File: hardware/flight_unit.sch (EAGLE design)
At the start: 26 parts, among them IC2 7805T, J2 CONN_20X2SHROUDED, T1 THERMISTOR-2,5, U1 4MB Flash, U2 4MB Flash, U3 4MB Flash

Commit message: Add files via upload
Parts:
- added X1, X2: S4B-ZR, con-jst:S4B-ZR
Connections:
- net GND: now also X1-2.1, X2-2.1
- net N$1: now also X1-1.1
- net N$4: now also X2-1.1
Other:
- moved on the sheet: D1
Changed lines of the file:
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@@
 <part name="C2" library="capacitor-wima" library_urn="urn:adsk.eagle:library:116" deviceset="C" device="2,5-3" package3d_urn="urn:adsk.eagle:package:5436/1" value="0.1uf"/>
 <part name="GND2" library="SparkFun-PowerSymbols" library_urn="urn:adsk.eagle:library:530" deviceset="GND" device=""/>
+<part name="X1" library="con-jst" library_urn="urn:adsk.eagle:library:156" deviceset="?4B-ZR" device="S" package3d_urn="urn:adsk.eagle:package:7641/1"/>
+<part name="X2" library="con-jst" library_urn="urn:adsk.eagle:library:156" deviceset="?4B-ZR" device="S" package3d_urn="urn:adsk.eagle:package:7641/1"/>
+<part name="GND9" library="SparkFun-PowerSymbols" library_urn="urn:adsk.eagle:library:530" deviceset="GND" device=""/>
+<part name="GND10" library="SparkFun-PowerSymbols" library_urn="urn:adsk.eagle:library:530" deviceset="GND" device=""/>
 </parts>
 <sheets>
@@
 </text>
 <text x="82.55" y="161.29" size="5.08" layer="97">Power Regulation and Supply</text>
-<text x="68.58" y="109.22" size="1.778" layer="91">ISS Power Source</text>
-<text x="114.3" y="81.28" size="1.778" layer="91">Backup Battery Input </text>
+<text x="78.74" y="116.84" size="1.778" layer="91">ISS Power Source</text>
+<text x="106.68" y="76.2" size="1.778" layer="91">Backup Battery Input </text>
 </plain>
 <instances>
@@
 <attribute name="SHEET" x="230.505" y="5.08" size="2.54" layer="94"/>
 </instance>
-<instance part="D1" gate="1" x="105.41" y="110.49" smashed="yes">
-<attribute name="NAME" x="107.95" y="110.9726" size="1.778" layer="95"/>
-<attribute name="VALUE" x="107.95" y="108.1786" size="1.778" layer="96"/>
+<instance part="D1" gate="1" x="110.49" y="110.49" smashed="yes">
+<attribute name="NAME" x="113.03" y="110.9726" size="1.778" layer="95"/>
+<attribute name="VALUE" x="113.03" y="108.1786" size="1.778" layer="96"/>
 </instance>
 <instance part="D2" gate="1" x="129.54" y="100.33" smashed="yes" rot="R90">
@@
 <instance part="GND2" gate="1" x="134.62" y="93.98" smashed="yes">
 <attribute name="VALUE" x="134.62" y="93.726" size="1.778" layer="96" align="top-center"/>
+</instance>
+<instance part="X1" gate="-1" x="116.84" y="86.36" smashed="yes" rot="MR0">
+<attribute name="NAME" x="115.824" y="85.598" size="1.524" layer="95" rot="MR0"/>
+<attribute name="VALUE" x="120.904" y="87.884" size="1.778" layer="96" rot="MR0"/>
+</instance>
+<instance part="X1" gate="-2" x="116.84" y="83.82" smashed="yes" rot="MR0">
+<attribute name="NAME" x="115.824" y="83.058" size="1.524" layer="95" rot="MR0"/>
+</instance>
+<instance part="X2" gate="-1" x="88.9" y="111.76" smashed="yes" rot="MR0">
+<attribute name="NAME" x="87.884" y="110.998" size="1.524" layer="95" rot="MR0"/>
+<attribute name="VALUE" x="92.964" y="113.284" size="1.778" layer="96" rot="MR0"/>
+</instance>
+<instance part="X2" gate="-2" x="88.9" y="109.22" smashed="yes" rot="MR0">
+<attribute name="NAME" x="87.884" y="108.458" size="1.524" layer="95" rot="MR0"/>
+</instance>
+<instance part="GND9" gate="1" x="96.52" y="106.68" smashed="yes">
+<attribute name="VALUE" x="96.52" y="106.426" size="1.778" layer="96" align="top-center"/>
+</instance>
+<instance part="GND10" gate="1" x="121.92" y="81.28" smashed="yes">
+<attribute name="VALUE" x="121.92" y="81.026" size="1.778" layer="96" align="top-center"/>
 </instance>
 </instances>
@@
 <wire x1="121.92" y1="95.25" x2="129.54" y2="95.25" width="0.1524" layer="91"/>
 <wire x1="129.54" y1="95.25" x2="129.54" y2="97.79" width="0.1524" layer="91"/>
-<wire x1="121.92" y1="95.25" x2="121.92" y2="83.82" width="0.1524" layer="91"/>
+<pinref part="X1" gate="-1" pin="1"/>
+<wire x1="121.92" y1="86.36" x2="121.92" y2="95.25" width="0.1524" layer="91"/>
 <junction x="121.92" y="95.25"/>
 </segment>
@@
 <pinref part="D1" gate="1" pin="C"/>
 <pinref part="R1" gate="G$1" pin="2"/>
-<wire x1="107.95" y1="110.49" x2="121.92" y2="110.49" width="0.1524" layer="91"/>
+<wire x1="113.03" y1="110.49" x2="121.92" y2="110.49" width="0.1524" layer="91"/>
 <wire x1="121.92" y1="110.49" x2="121.92" y2="105.41" width="0.1524" layer="91"/>
 <junction x="121.92" y="110.49"/>
@@
 </segment>
 </net>
-<net name="N$4" class="0">
-<segment>
-<pinref part="D1" gate="1" pin="A"/>
-<wire x1="91.44" y1="110.49" x2="102.87" y2="110.49" width="0.1524" layer="91"/>
-</segment>
-</net>
 <net name="+3V3" class="0">
 <segment>
@@
 <wire x1="134.62" y1="99.06" x2="134.62" y2="96.52" width="0.1524" layer="91"/>
 </segment>
+<segment>
+<pinref part="X2" gate="-2" pin="1"/>
+<pinref part="GND9" gate="1" pin="GND"/>
+<wire x1="93.98" y1="109.22" x2="96.52" y2="109.22" width="0.1524" layer="91"/>
+</segment>
+<segment>
+<pinref part="GND10" gate="1" pin="GND"/>
+<pinref part="X1" gate="-2" pin="1"/>
+</segment>
 </net>
 <net name="N$9" class="0">
@@
 </segment>
 </net>
+<net name="N$4" class="0">
+<segment>
+<pinref part="X2" gate="-1" pin="1"/>
+<pinref part="D1" gate="1" pin="A"/>
+<wire x1="93.98" y1="111.76" x2="107.95" y2="111.76" width="0.1524" layer="91"/>
+<wire x1="107.95" y1="111.76" x2="107.95" y2="110.49" width="0.1524" layer="91"/>
+</segment>
+</net>

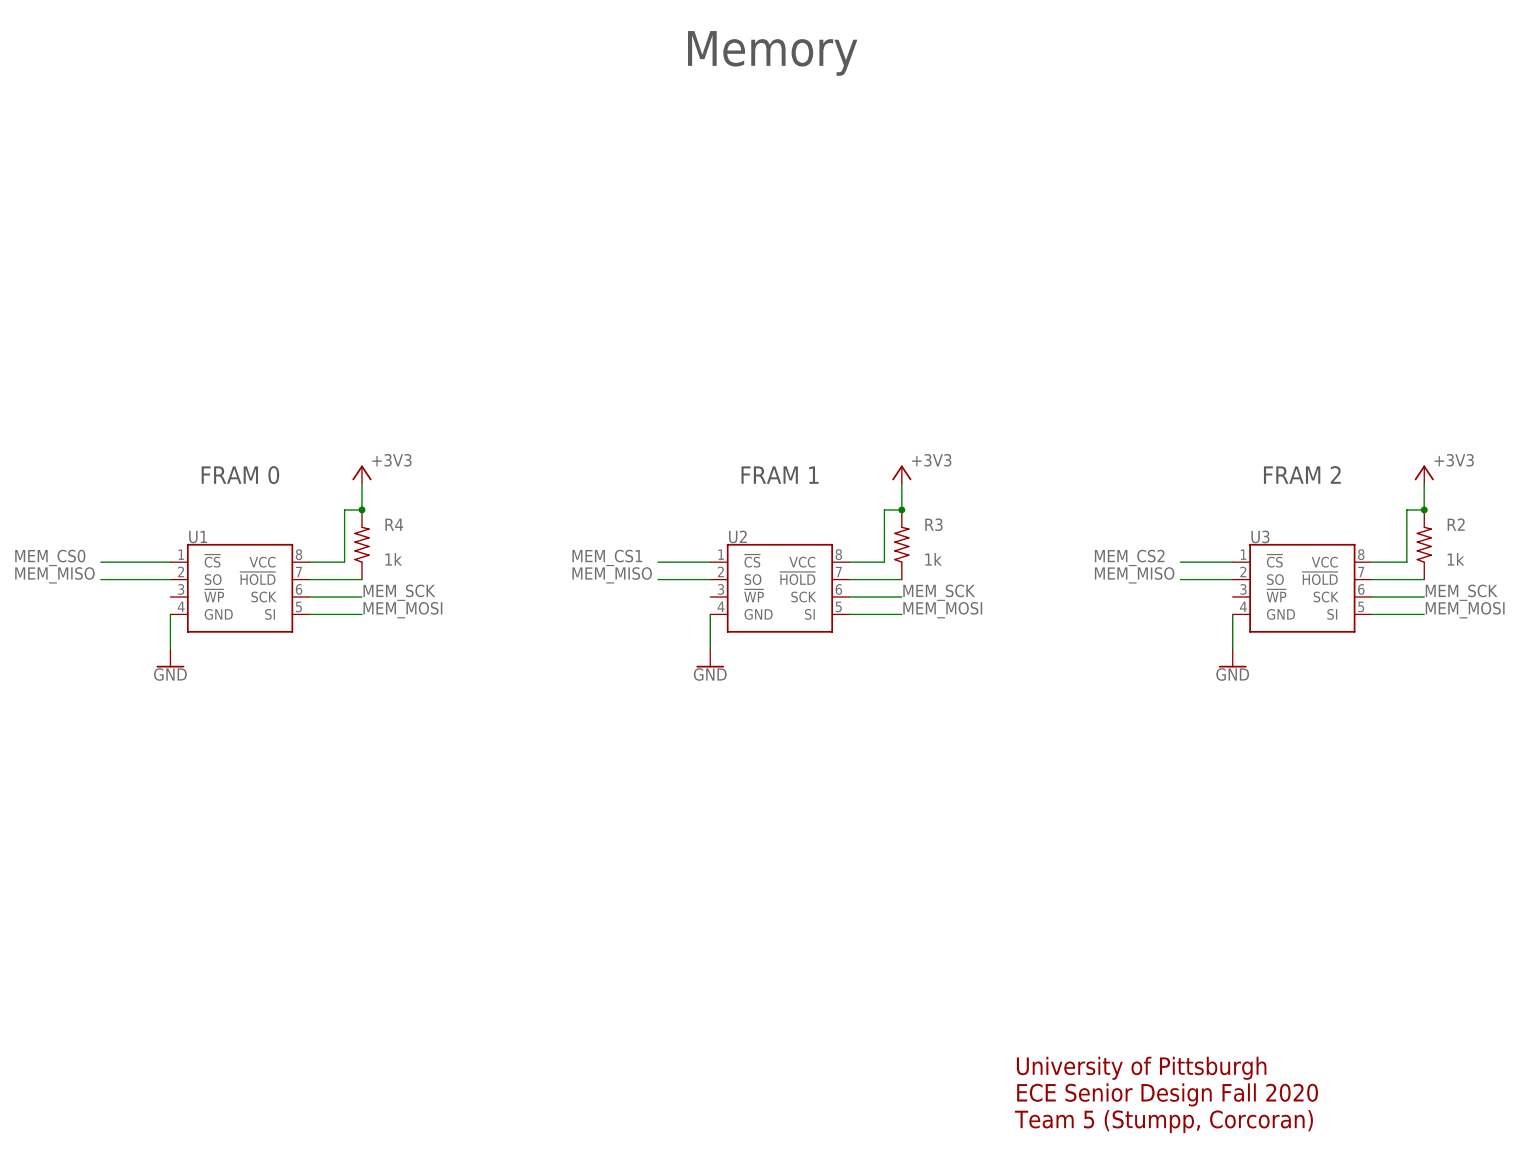
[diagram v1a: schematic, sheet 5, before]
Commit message: Added decoupling caps to memory schematic
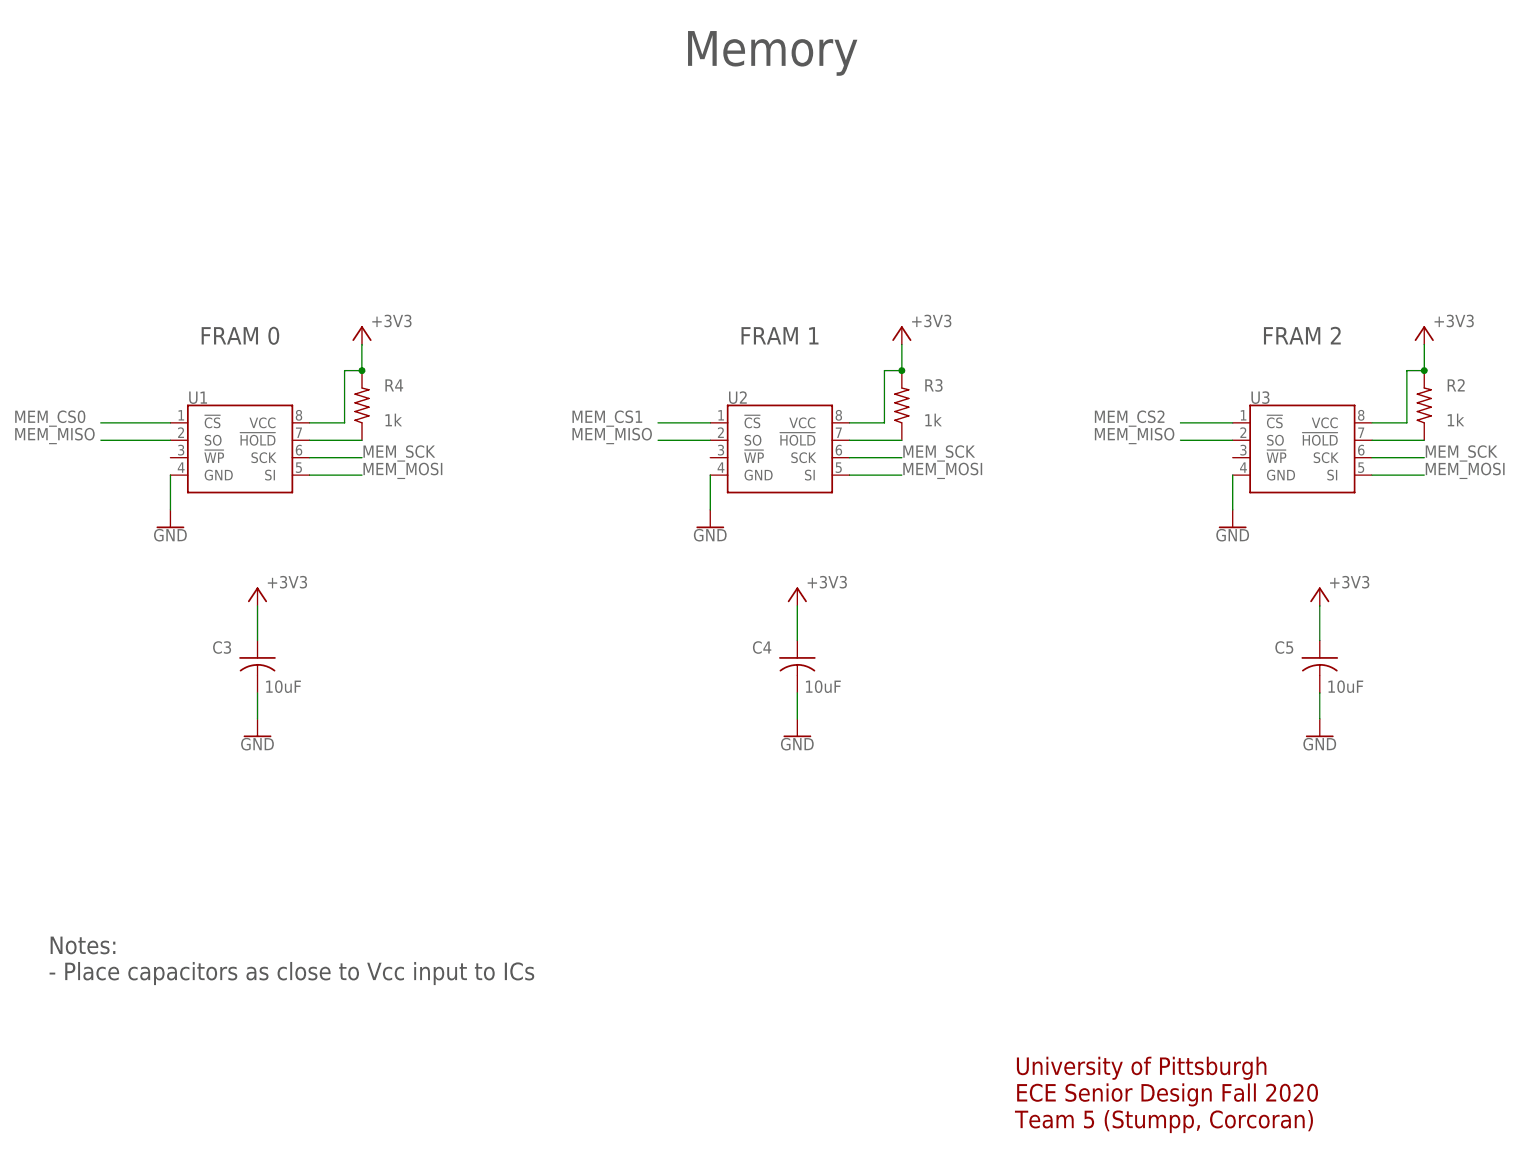
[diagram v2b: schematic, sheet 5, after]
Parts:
- added C3, C4, C5: 10uF, adafruit:C-US025-040X050
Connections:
- net +3V3: now also C3.1, C4.1, C5.1
- net GND: now also C3.2, C4.2, C5.2
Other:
- note added: "Notes: - Place capacitors as close to Vcc input to ICs"
- moved on the sheet: R2, R3, R4, U1, U2, U3

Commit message: updates to schematic and preliminary board work
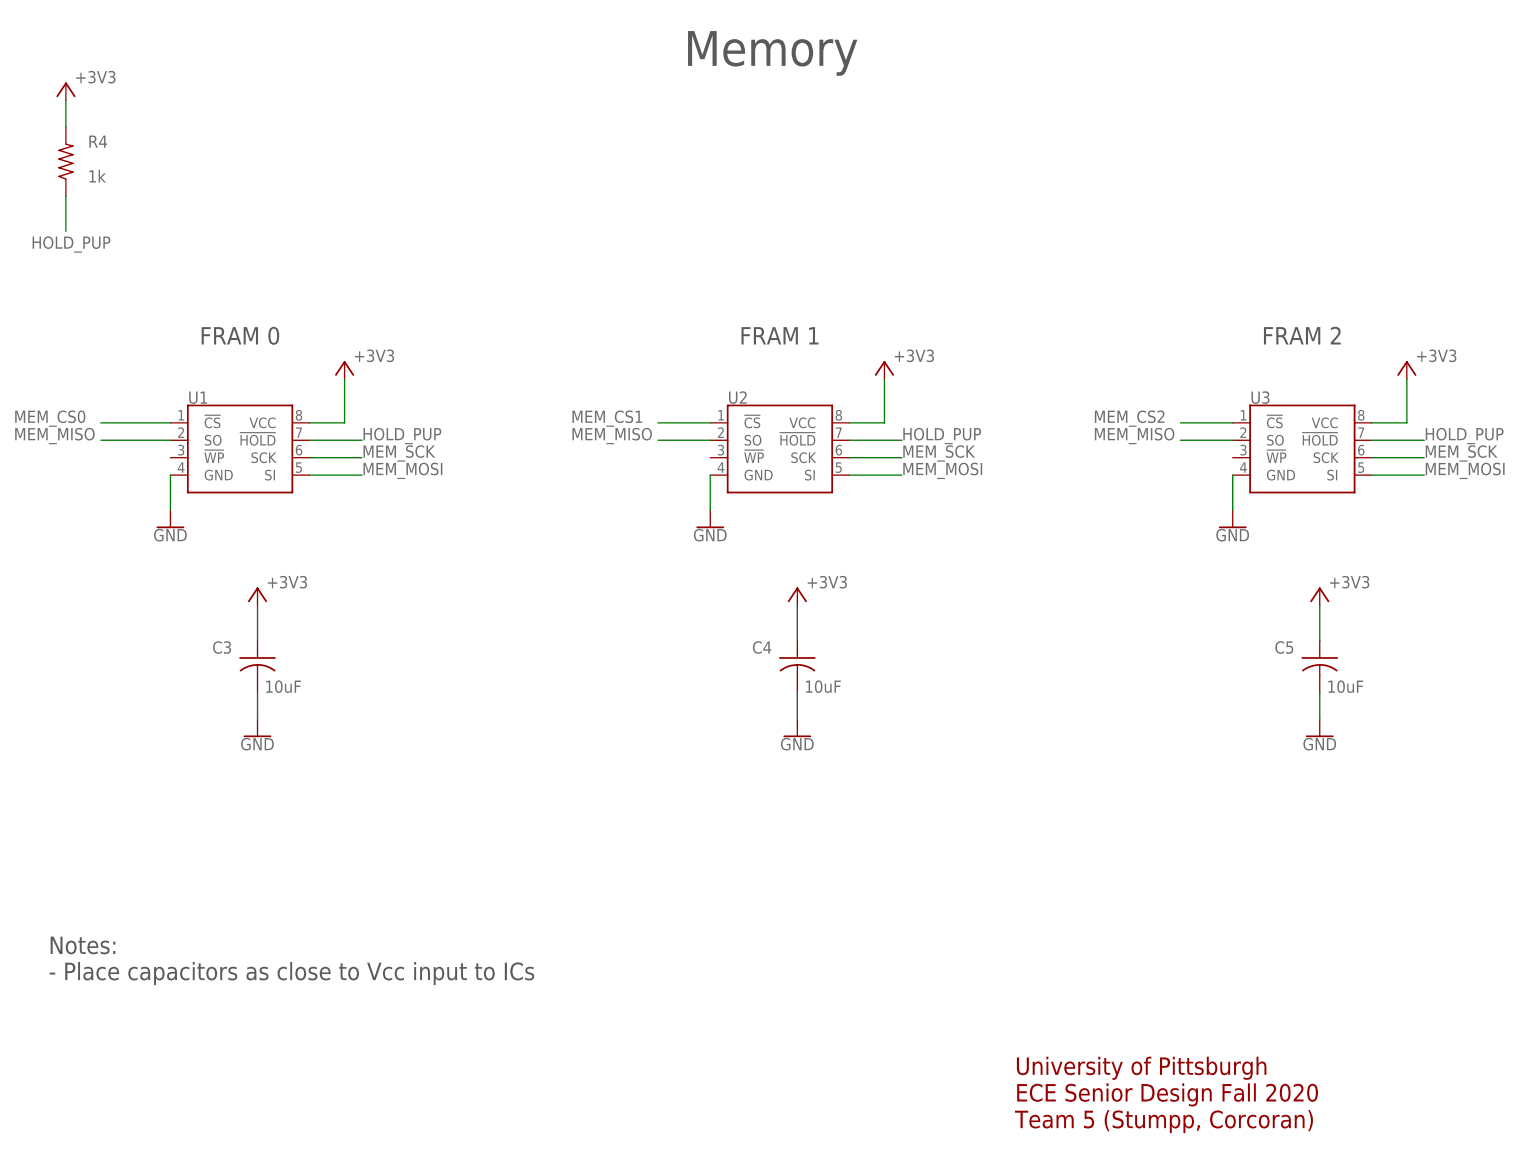
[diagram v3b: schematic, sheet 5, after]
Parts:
- removed R2, R3: 1k, resistor:R-US_R1210
- renumbered J2 to J1
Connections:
- removed net N$3: R2.1, U3.!HOLD
- removed net N$5: R4.1, U1.!HOLD
- removed net N$6: R3.1, U2.!HOLD
- new net HOLD_PUP: R4.1, U1.!HOLD, U2.!HOLD, U3.!HOLD
- net +3V3: no longer R2.2, R3.2
- net GND: now also J1.10, J1.13, J1.19, J1.26, J1.29, J1.33, J1.40, J1.5; no longer J1.14, J1.20, J1.25, J1.30, J1.34, J1.39, J1.6, J1.9
- net IIC_SCL: now also J1.30; no longer J1.29
- net IIC_SDA: now also J1.8; no longer J1.7
- net SC_3V3: now also J1.18, J1.2; no longer J1.1, J1.17
- net SC_5V0: now also J1.1, J1.3; no longer J1.2, J1.4
- net SC_D0: now also J1.7; no longer J1.8
- net SC_D1: now also J1.11; no longer J1.12
- net SC_D2: now also J1.15; no longer J1.16
- net SC_D3: now also J1.21; no longer J1.22
- net SC_D4: now also J1.35; no longer J1.36
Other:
- moved on the sheet: R4

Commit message: working on board layout
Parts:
- added H1, H2: SEW_HOLE, SparkFun-Retired:SEW_HOLE
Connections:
- net GND: now also H1.P$1, H2.P$1
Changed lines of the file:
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@@
 <part name="+3V5" library="supply1" deviceset="+3V3" device=""/>
 <part name="+3V11" library="supply1" deviceset="+3V3" device=""/>
+<part name="H1" library="SparkFun-Retired" deviceset="SEW_HOLE" device=""/>
+<part name="H2" library="SparkFun-Retired" deviceset="SEW_HOLE" device=""/>
+<part name="GND15" library="SparkFun-PowerSymbols" library_urn="urn:adsk.eagle:library:530" deviceset="GND" device=""/>
 </parts>
 <sheets>
@@
 <attribute name="VALUE" x="121.92" y="81.026" size="1.778" layer="96" align="top-center"/>
 </instance>
+<instance part="H1" gate="G$1" x="223.52" y="109.22" smashed="yes">
+<attribute name="NAME" x="220.98" y="112.014" size="1.778" layer="95" font="vector"/>
+<attribute name="VALUE" x="220.98" y="106.426" size="1.778" layer="96" font="vector" align="top-left"/>
+</instance>
+<instance part="H2" gate="G$1" x="223.52" y="96.52" smashed="yes">
+<attribute name="NAME" x="220.98" y="99.314" size="1.778" layer="95" font="vector"/>
+<attribute name="VALUE" x="220.98" y="93.726" size="1.778" layer="96" font="vector" align="top-left"/>
+</instance>
+<instance part="GND15" gate="1" x="215.9" y="78.74" smashed="yes">
+<attribute name="VALUE" x="215.9" y="78.486" size="1.778" layer="96" align="top-center"/>
+</instance>
 </instances>
 <busses>
@@
 <pinref part="X1" gate="-2" pin="1"/>
 </segment>
-</net>
+<segment>
+<pinref part="GND15" gate="1" pin="GND"/>
+<wire x1="215.9" y1="81.28" x2="215.9" y2="96.52" width="0.1524" layer="91"/>
+<pinref part="H1" gate="G$1" pin="P$1"/>
+<wire x1="218.44" y1="109.22" x2="215.9" y2="109.22" width="0.1524" layer="91"/>
+<wire x1="215.9" y1="109.22" x2="215.9" y2="96.52" width="0.1524" layer="91"/>
+<pinref part="H2" gate="G$1" pin="P$1"/>
+<wire x1="215.9" y1="96.52" x2="218.44" y2="96.52" width="0.1524" layer="91"/>
+</segment>
+</net>
